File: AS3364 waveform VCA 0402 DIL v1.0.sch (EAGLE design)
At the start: 48 parts, among them IC1 TL072JD, IC2 TL072JD

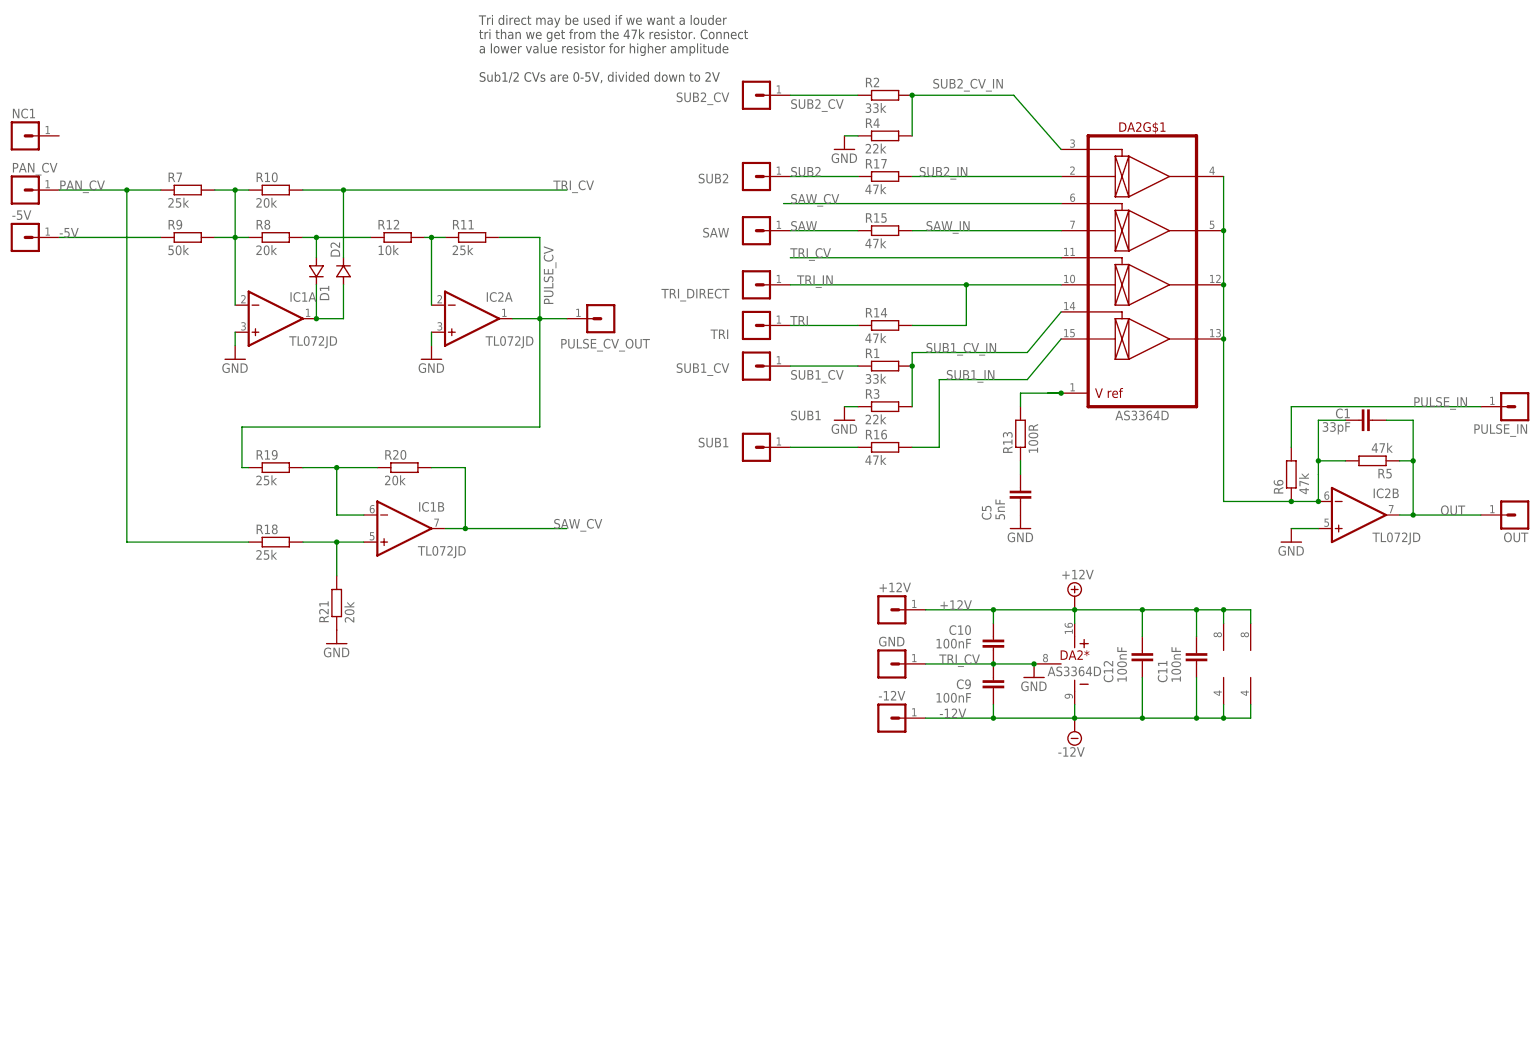
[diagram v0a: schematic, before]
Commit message: Almost finished bom/cpl
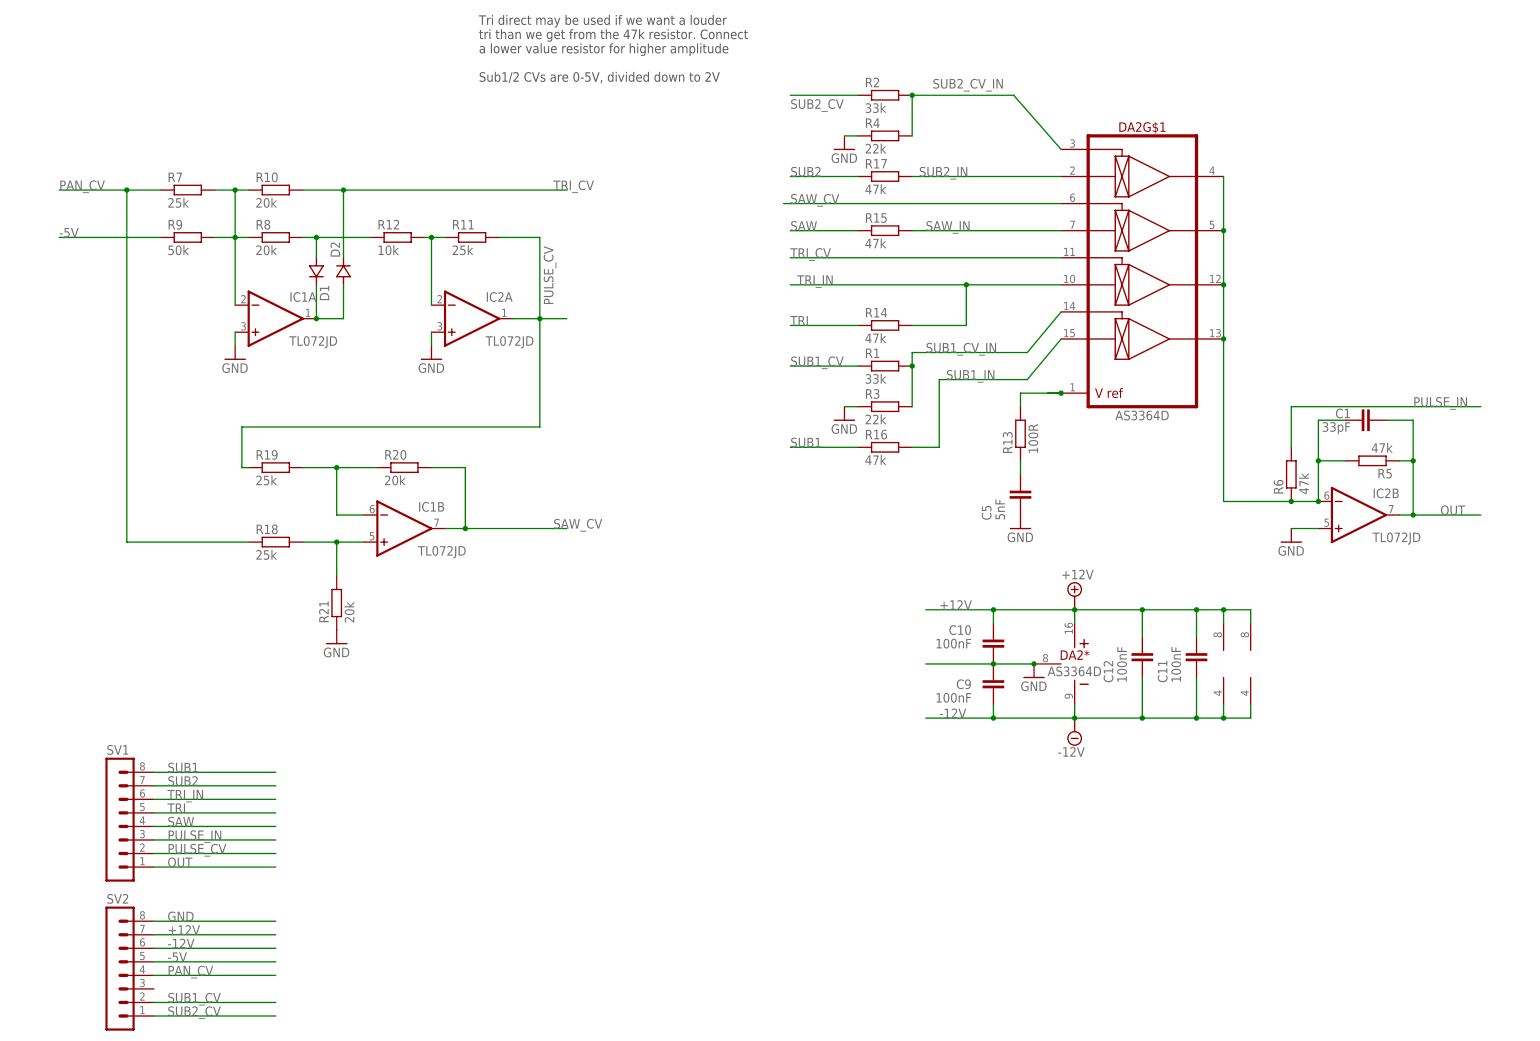
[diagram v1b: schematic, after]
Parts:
- removed +12V, -12V, -5V, GND, NC1, OUT, PAN_CV, PULSE_CV_OUT, PULSE_IN, SAW, SUB1, SUB1_CV, SUB2, SUB2_CV, TRI, TRI_DIRECT: (no value), joakim:MA01-1JP
- added SV1, SV2: (no value), joakim:MA08-1JP
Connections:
- net +12V: now also SV2.7; no longer +12V.1
- net -12V: now also SV2.6; no longer -12V.1
- net -5V: now also SV2.5; no longer -5V.1
- net GND: now also SV2.8; no longer GND.1
- net OUT: now also SV1.1; no longer OUT.1
- net PAN_CV: now also SV2.4; no longer PAN_CV.1
- net PULSE_CV: now also SV1.2; no longer PULSE_CV_OUT.1
- net PULSE_IN: now also SV1.3; no longer PULSE_IN.1
- net SAW: now also SV1.4; no longer SAW.1
- net SUB1: now also SV1.8; no longer SUB1.1
- net SUB1_CV: now also SV2.2; no longer SUB1_CV.1
- net SUB2: now also SV1.7; no longer SUB2.1
- net SUB2_CV: now also SV2.1; no longer SUB2_CV.1
- net TRI: now also SV1.5; no longer TRI.1
- net TRI_IN: now also SV1.6; no longer TRI_DIRECT.1
